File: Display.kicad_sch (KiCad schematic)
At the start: 0 parts

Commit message: PMIC DCDC
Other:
- title: Leaf RV1126 Power -> Leaf RV1126 PMIC RK809
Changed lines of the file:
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@@
   (paper "A4")
   (title_block
-    (title "Leaf RV1126 Power")
+    (title "Leaf RV1126 PMIC RK809")
     (date "2023-02-23")
     (rev "1")

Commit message: updated: PMIC codec
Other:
- title: Leaf RV1126 PMIC RK809 -> Leaf RV1126 PMIC RK809 Codec
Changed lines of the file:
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@@
   (paper "A4")
   (title_block
-    (title "Leaf RV1126 PMIC RK809")
-    (date "2023-02-23")
+    (title "Leaf RV1126 PMIC RK809 Codec")
+    (date "2023-02-25")
     (rev "1")
     (company "Qingdao IotPi Information Technology")

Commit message: updated: titles
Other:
- title: Leaf RV1126 PMIC RK809 Codec -> Leaf RV1126 RK809 Display
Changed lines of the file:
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@@
   (paper "A4")
   (title_block
-    (title "Leaf RV1126 PMIC RK809 Codec")
+    (title "Leaf RV1126 RK809 Display")
     (date "2023-02-25")
     (rev "1")

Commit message: MIPI-DSI block
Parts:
- added U1: rv1126/rv1109, symbol CPU_Rockchip:rv1126_rv1109

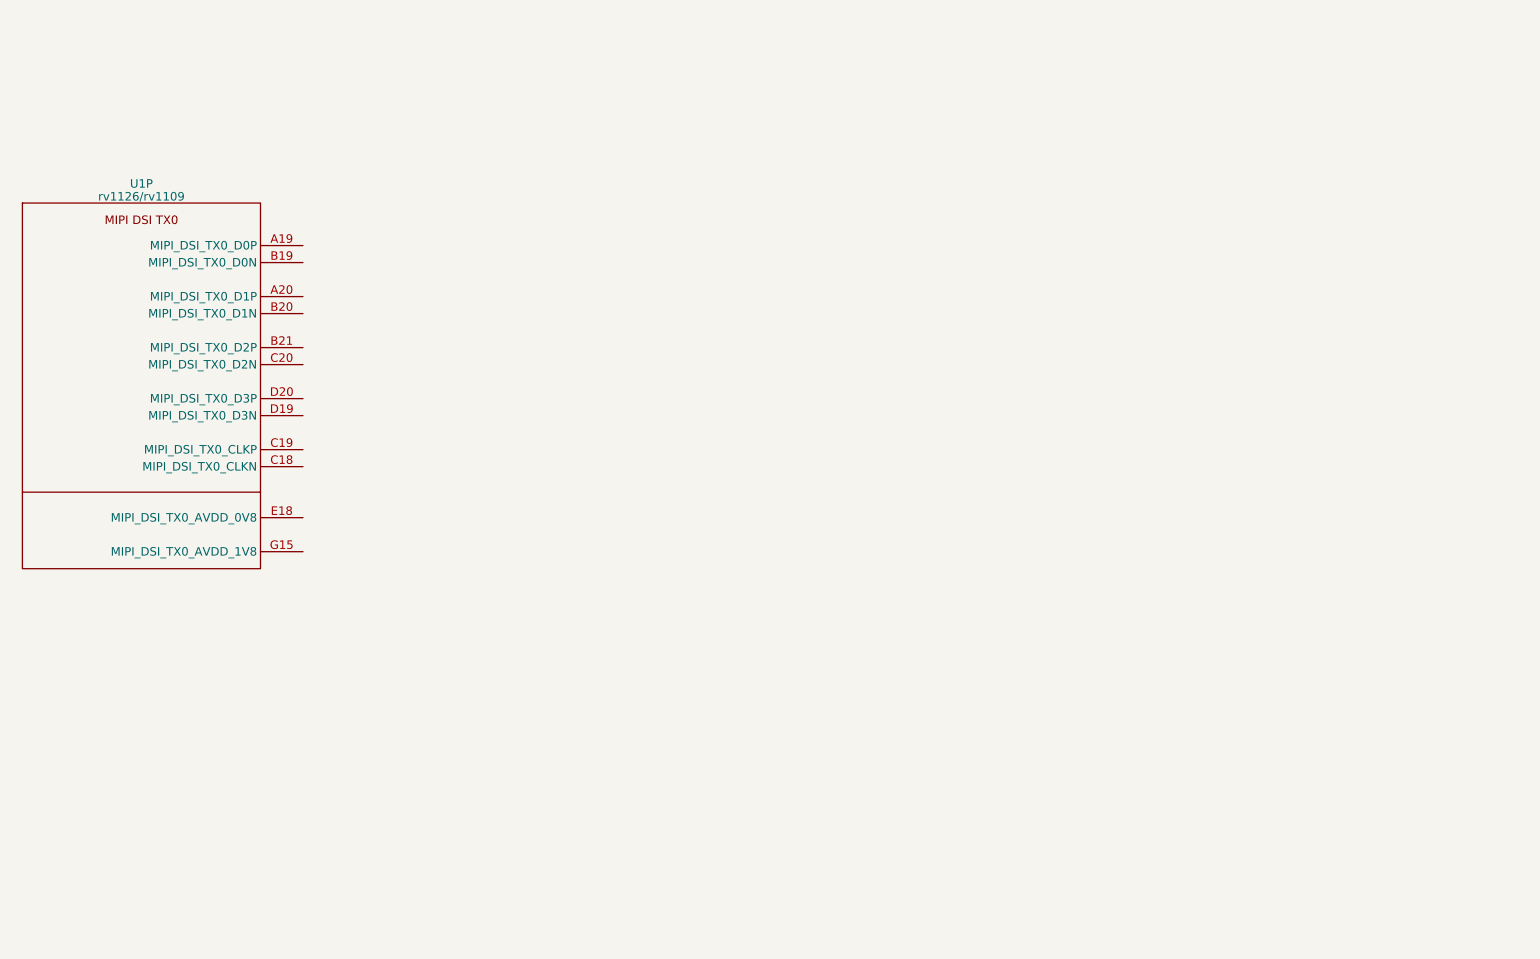
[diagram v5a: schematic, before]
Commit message: Updated:
Added Display
Rename DDR to DDR3
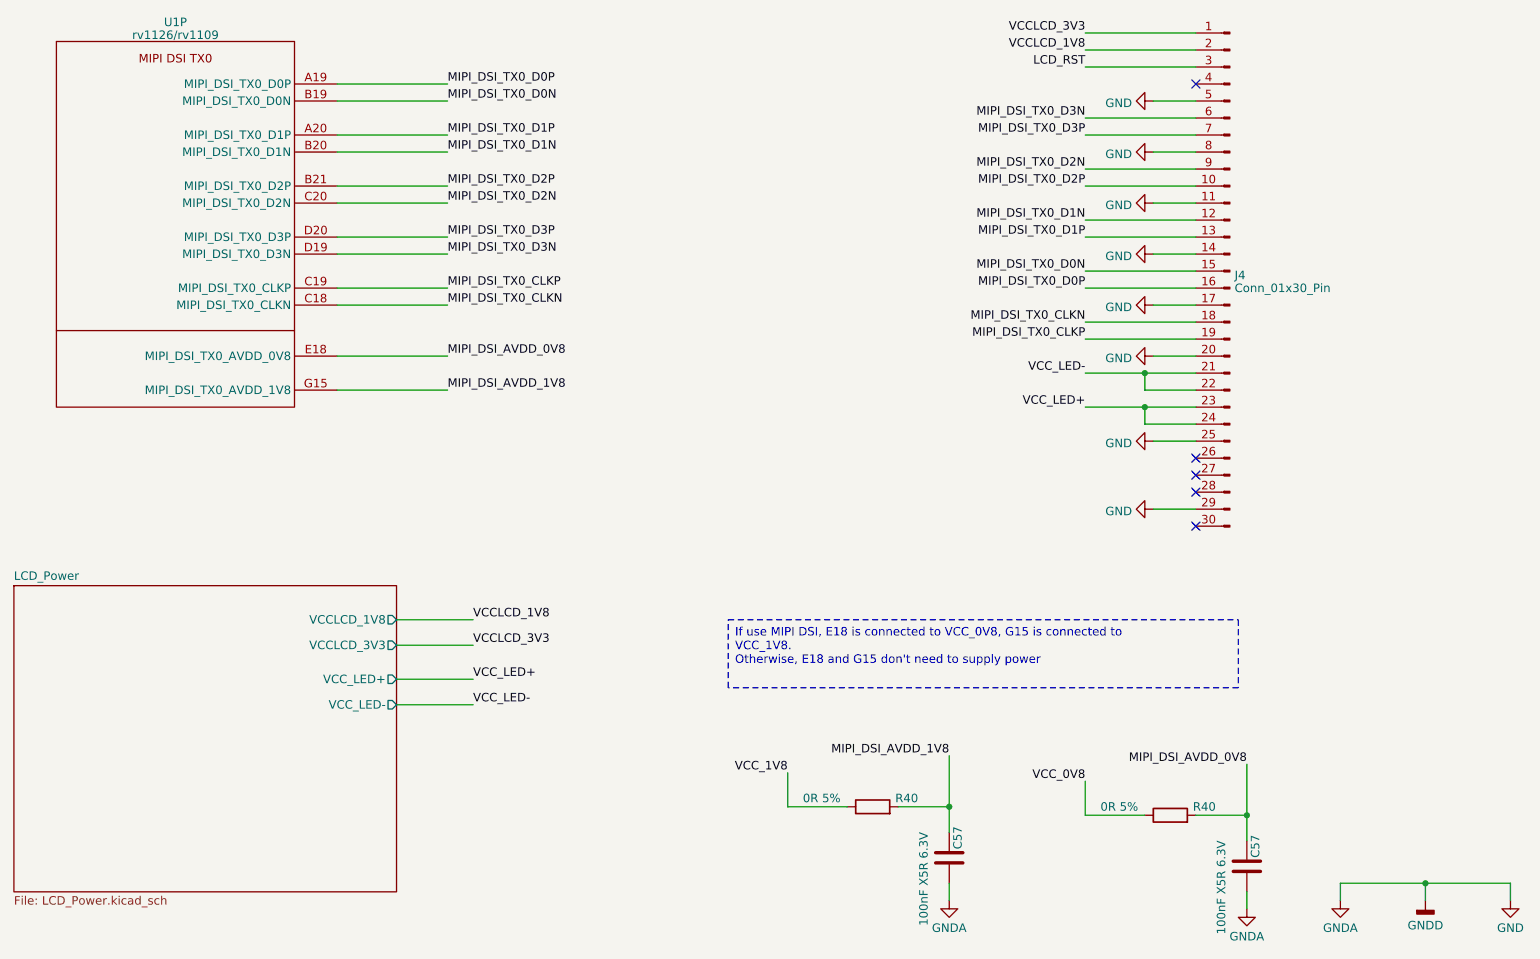
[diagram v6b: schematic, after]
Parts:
- added C57 (x2): 100nF X5R 6.3V, Capacitor_SMD:C_0201_0603Metric, symbol Device:C
- added J4: Conn_01x30_Pin, symbol Connector:Conn_01x30_Pin
- added R40 (x2): 0R 5%, Resistor_SMD:R_0402_1005Metric, symbol Device:R
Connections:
- net MIPI_DSI_TX0_D0P: now reaches U1.A19 (MIPI_DSI_TX0_D0P)
- net MIPI_DSI_TX0_D0P: now also J4.16 (Pin_16)
- net MIPI_DSI_TX0_D1P: now reaches U1.A20 (MIPI_DSI_TX0_D1P)
- net MIPI_DSI_TX0_D1P: now also J4.13 (Pin_13)
- net MIPI_DSI_TX0_D0N: now reaches U1.B19 (MIPI_DSI_TX0_D0N)
- net MIPI_DSI_TX0_D0N: now also J4.15 (Pin_15)
- net MIPI_DSI_TX0_D1N: now reaches U1.B20 (MIPI_DSI_TX0_D1N)
- net MIPI_DSI_TX0_D1N: now also J4.12 (Pin_12)
- net MIPI_DSI_TX0_D2P: now reaches U1.B21 (MIPI_DSI_TX0_D2P)
- net MIPI_DSI_TX0_D2P: now also J4.10 (Pin_10)
- net MIPI_DSI_TX0_CLKN: now reaches U1.C18 (MIPI_DSI_TX0_CLKN)
- net MIPI_DSI_TX0_CLKN: now also J4.18 (Pin_18)
- net MIPI_DSI_TX0_CLKP: now reaches U1.C19 (MIPI_DSI_TX0_CLKP)
- net MIPI_DSI_TX0_CLKP: now also J4.19 (Pin_19)
- net MIPI_DSI_TX0_D2N: now reaches U1.C20 (MIPI_DSI_TX0_D2N)
- net MIPI_DSI_TX0_D2N: now also J4.9 (Pin_9)
- net MIPI_DSI_TX0_D3N: now reaches U1.D19 (MIPI_DSI_TX0_D3N)
- net MIPI_DSI_TX0_D3N: now also J4.6 (Pin_6)
- net MIPI_DSI_TX0_D3P: now reaches U1.D20 (MIPI_DSI_TX0_D3P)
- net MIPI_DSI_TX0_D3P: now also J4.7 (Pin_7)
- net MIPI_DSI_AVDD_0V8: now reaches U1.E18 (MIPI_DSI_TX0_AVDD_0V8)
- net MIPI_DSI_AVDD_0V8: now also C57.1, R40.2
- net MIPI_DSI_AVDD_1V8: now reaches U1.G15 (MIPI_DSI_TX0_AVDD_1V8)
- net MIPI_DSI_AVDD_1V8: now also C57.1, R40.2
- new net GND: C57.2, C57.2, J4.11 (Pin_11), J4.14 (Pin_14), J4.17 (Pin_17), J4.20 (Pin_20), J4.25 (Pin_25), J4.29 (Pin_29), J4.5 (Pin_5), J4.8 (Pin_8)
- new net LCD_RST: J4.3 (Pin_3)
- new net VCCLCD_1V8: J4.2 (Pin_2)
- new net VCCLCD_3V3: J4.1 (Pin_1)
- new net VCC_0V8: R40.1
- new net VCC_1V8: R40.1
- new net VCC_LED+: J4.23 (Pin_23), J4.24 (Pin_24)
- new net VCC_LED-: J4.21 (Pin_21), J4.22 (Pin_22)
- no-connect marks 0 -> 5
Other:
- added sheet LCD_Power (LCD_Power.kicad_sch)
- moved on the sheet: U1P

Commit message: updated footprints
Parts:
- U1: footprint (none) -> Rockchip_SoC:Rockchip_RV1126_FCCSP409LD_14.0x14.0mm
- renumbered J4 to J3
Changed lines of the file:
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@@
         )
         (path "/e3b58043-16a3-43c8-9fad-9c9784eebfa4/abba4c44-e9bc-404f-bbc8-3409461eb15e"
-          (reference "#PWR0109") (unit 1)
+          (reference "#PWR032") (unit 1)
         )
       )
@@
         )
         (path "/e3b58043-16a3-43c8-9fad-9c9784eebfa4/abba4c44-e9bc-404f-bbc8-3409461eb15e"
-          (reference "#PWR0110") (unit 1)
+          (reference "#PWR041") (unit 1)
         )
       )
@@
         )
         (path "/e3b58043-16a3-43c8-9fad-9c9784eebfa4/abba4c44-e9bc-404f-bbc8-3409461eb15e"
-          (reference "C127") (unit 1)
+          (reference "C22") (unit 1)
         )
       )
@@
   (symbol (lib_id "power:GND") (at 214.63 96.52 270) (unit 1)
     (in_bom yes) (on_board yes) (dnp no) (fields_autoplaced)
-    (property "Reference" "#PWR0121" (at 208.28 96.52 0)
+    (property "Reference" "#PWR040" (at 208.28 96.52 0)
       (effects (font (size 1.27 1.27)) hide)
     )
@@
       (project "leaf"
         (path "/e3b58043-16a3-43c8-9fad-9c9784eebfa4/abba4c44-e9bc-404f-bbc8-3409461eb15e"
-          (reference "#PWR0121") (unit 1)
+          (reference "#PWR040") (unit 1)
         )
       )
@@
         )
         (path "/e3b58043-16a3-43c8-9fad-9c9784eebfa4/abba4c44-e9bc-404f-bbc8-3409461eb15e"
-          (reference "R63") (unit 1)
+          (reference "R25") (unit 1)
         )
       )
@@
   (symbol (lib_id "power:GND") (at 214.63 35.56 270) (unit 1)
     (in_bom yes) (on_board yes) (dnp no) (fields_autoplaced)
-    (property "Reference" "#PWR0118" (at 208.28 35.56 0)
+    (property "Reference" "#PWR033" (at 208.28 35.56 0)
       (effects (font (size 1.27 1.27)) hide)
     )
@@
       (project "leaf"
         (path "/e3b58043-16a3-43c8-9fad-9c9784eebfa4/abba4c44-e9bc-404f-bbc8-3409461eb15e"
-          (reference "#PWR0118") (unit 1)
+          (reference "#PWR033") (unit 1)
         )
       )
@@
         )
         (path "/e3b58043-16a3-43c8-9fad-9c9784eebfa4/abba4c44-e9bc-404f-bbc8-3409461eb15e"
-          (reference "#PWR0112") (unit 1)
+          (reference "#PWR043") (unit 1)
         )
       )
@@
       (effects (font (size 1.27 1.27)))
     )
-    (property "Footprint" "" (at 100.33 83.82 0)
+    (property "Footprint" "Rockchip_SoC:Rockchip_RV1126_FCCSP409LD_14.0x14.0mm" (at 100.33 83.82 0)
       (effects (font (size 1.27 1.27)) hide)
     )
@@
         )
         (path "/e3b58043-16a3-43c8-9fad-9c9784eebfa4/abba4c44-e9bc-404f-bbc8-3409461eb15e"
-          (reference "R62") (unit 1)
+          (reference "R24") (unit 1)
         )
       )
@@
   (symbol (lib_id "power:GND") (at 214.63 66.04 270) (unit 1)
     (in_bom yes) (on_board yes) (dnp no) (fields_autoplaced)
-    (property "Reference" "#PWR0114" (at 208.28 66.04 0)
+    (property "Reference" "#PWR037" (at 208.28 66.04 0)
       (effects (font (size 1.27 1.27)) hide)
     )
@@
       (project "leaf"
         (path "/e3b58043-16a3-43c8-9fad-9c9784eebfa4/abba4c44-e9bc-404f-bbc8-3409461eb15e"
-          (reference "#PWR0114") (unit 1)
+          (reference "#PWR037") (unit 1)
         )
       )
@@
   (symbol (lib_id "power:GND") (at 214.63 86.36 270) (unit 1)
     (in_bom yes) (on_board yes) (dnp no) (fields_autoplaced)
-    (property "Reference" "#PWR0120" (at 208.28 86.36 0)
+    (property "Reference" "#PWR039" (at 208.28 86.36 0)
       (effects (font (size 1.27 1.27)) hide)
     )
@@
       (project "leaf"
         (path "/e3b58043-16a3-43c8-9fad-9c9784eebfa4/abba4c44-e9bc-404f-bbc8-3409461eb15e"
-          (reference "#PWR0120") (unit 1)
+          (reference "#PWR039") (unit 1)
         )
       )
@@
         )
         (path "/e3b58043-16a3-43c8-9fad-9c9784eebfa4/abba4c44-e9bc-404f-bbc8-3409461eb15e"
-          (reference "C126") (unit 1)
+          (reference "C21") (unit 1)
         )
       )
@@
   (symbol (lib_id "power:GND") (at 214.63 43.18 270) (unit 1)
     (in_bom yes) (on_board yes) (dnp no) (fields_autoplaced)
-    (property "Reference" "#PWR0116" (at 208.28 43.18 0)
+    (property "Reference" "#PWR034" (at 208.28 43.18 0)
       (effects (font (size 1.27 1.27)) hide)
     )
@@
       (project "leaf"
         (path "/e3b58043-16a3-43c8-9fad-9c9784eebfa4/abba4c44-e9bc-404f-bbc8-3409461eb15e"
-          (reference "#PWR0116") (unit 1)
+          (reference "#PWR034") (unit 1)
         )
       )
@@
   (symbol (lib_id "power:GND") (at 214.63 50.8 270) (unit 1)
     (in_bom yes) (on_board yes) (dnp no) (fields_autoplaced)
-    (property "Reference" "#PWR0117" (at 208.28 50.8 0)
+    (property "Reference" "#PWR035" (at 208.28 50.8 0)
       (effects (font (size 1.27 1.27)) hide)
     )
@@
       (project "leaf"
         (path "/e3b58043-16a3-43c8-9fad-9c9784eebfa4/abba4c44-e9bc-404f-bbc8-3409461eb15e"
-          (reference "#PWR0117") (unit 1)
+          (reference "#PWR035") (unit 1)
         )
       )
@@
   (symbol (lib_id "power:GND") (at 214.63 58.42 270) (unit 1)
     (in_bom yes) (on_board yes) (dnp no) (fields_autoplaced)
-    (property "Reference" "#PWR0115" (at 208.28 58.42 0)
+    (property "Reference" "#PWR036" (at 208.28 58.42 0)
       (effects (font (size 1.27 1.27)) hide)
     )
@@
       (project "leaf"
         (path "/e3b58043-16a3-43c8-9fad-9c9784eebfa4/abba4c44-e9bc-404f-bbc8-3409461eb15e"
-          (reference "#PWR0115") (unit 1)
+          (reference "#PWR036") (unit 1)
         )
       )
@@
   (symbol (lib_id "Connector:Conn_01x30_Pin") (at 226.06 60.96 0) (mirror y) (unit 1)
     (in_bom yes) (on_board yes) (dnp no) (fields_autoplaced)
-    (property "Reference" "J4" (at 226.7712 61.5863 0)
+    (property "Reference" "J3" (at 226.7712 61.5863 0)
       (effects (font (size 1.27 1.27)) (justify right))
     )
@@
       (project "leaf"
         (path "/e3b58043-16a3-43c8-9fad-9c9784eebfa4/abba4c44-e9bc-404f-bbc8-3409461eb15e"
-          (reference "J4") (unit 1)
+          (reference "J3") (unit 1)
         )
       )
@@
         )
         (path "/e3b58043-16a3-43c8-9fad-9c9784eebfa4/abba4c44-e9bc-404f-bbc8-3409461eb15e"
-          (reference "#PWR0111") (unit 1)
+          (reference "#PWR042") (unit 1)
         )
       )
@@
   (symbol (lib_id "power:GND") (at 214.63 73.66 270) (unit 1)
     (in_bom yes) (on_board yes) (dnp no) (fields_autoplaced)
-    (property "Reference" "#PWR0119" (at 208.28 73.66 0)
+    (property "Reference" "#PWR038" (at 208.28 73.66 0)
       (effects (font (size 1.27 1.27)) hide)
     )
@@
       (project "leaf"
         (path "/e3b58043-16a3-43c8-9fad-9c9784eebfa4/abba4c44-e9bc-404f-bbc8-3409461eb15e"
-          (reference "#PWR0119") (unit 1)
+          (reference "#PWR038") (unit 1)
         )
       )
@@
         )
         (path "/e3b58043-16a3-43c8-9fad-9c9784eebfa4/abba4c44-e9bc-404f-bbc8-3409461eb15e"
-          (reference "#PWR0113") (unit 1)
-        )
-      )
+          (reference "#PWR044") (unit 1)
+        )
+      )

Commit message: updated Capacitors
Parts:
- C57: LCSC (none) -> C76934; Model (none) -> GRM033R61A104KE15D; Vendor (none) -> muRata(村田)
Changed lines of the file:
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@@
+      (effects (font (size 1.27 1.27)) hide)
+    )
+    (property "Description" "容值: 100nF 精度: ±10% 额定电压: 10V 材质(温度系数): X5R 材质:X5R" (at 228.6 149.86 0)
+      (effects (font (size 1.27 1.27)) hide)
+    )
+    (property "LCSC" "C76934" (at 228.6 149.86 0)
+      (effects (font (size 1.27 1.27)) hide)
+    )
+    (property "Model" "GRM033R61A104KE15D" (at 228.6 149.86 0)
+      (effects (font (size 1.27 1.27)) hide)
+    )
+    (property "Vendor" "muRata(村田)" (at 228.6 149.86 0)
       (effects (font (size 1.27 1.27)) hide)
     )
@@
       (effects (font (size 1.27 1.27)) hide)
     )
+    (property "Description" "容值: 100nF 精度: ±10% 额定电压: 10V 材质(温度系数): X5R 材质:X5R" (at 184.15 148.59 0)
+      (effects (font (size 1.27 1.27)) hide)
+    )
+    (property "LCSC" "C76934" (at 184.15 148.59 0)
+      (effects (font (size 1.27 1.27)) hide)
+    )
+    (property "Model" "GRM033R61A104KE15D" (at 184.15 148.59 0)
+      (effects (font (size 1.27 1.27)) hide)
+    )
+    (property "Vendor" "muRata(村田)" (at 184.15 148.59 0)
+      (effects (font (size 1.27 1.27)) hide)
+    )
